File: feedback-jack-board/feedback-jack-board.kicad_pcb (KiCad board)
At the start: 2 copper layers, 80 x 36 mm, 6 parts, among them J1 Out, J2 Ret, J3 In, J4 Snd, J5 908140508, J6 Barrel_Jack_Switch

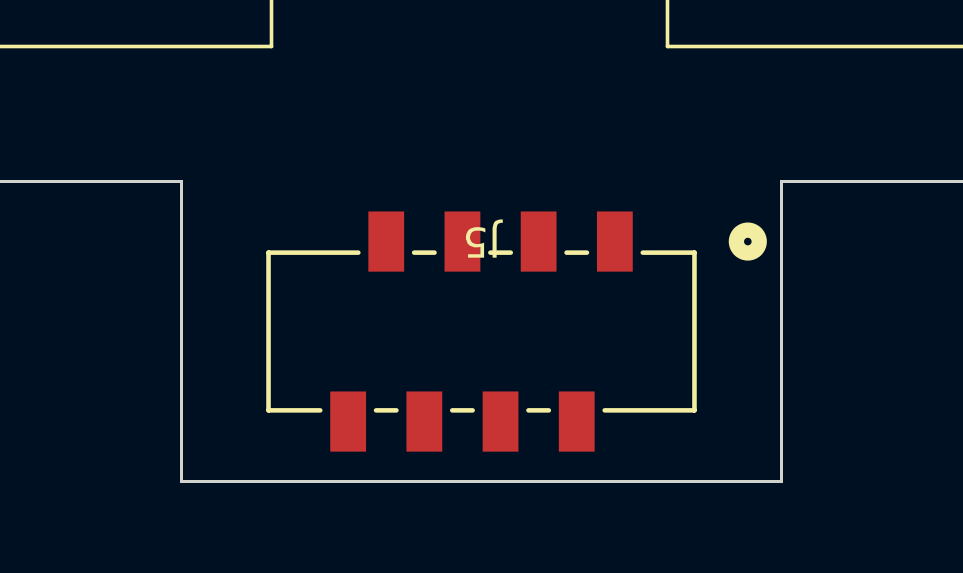
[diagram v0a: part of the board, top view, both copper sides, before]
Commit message: Rotate molex connector properly
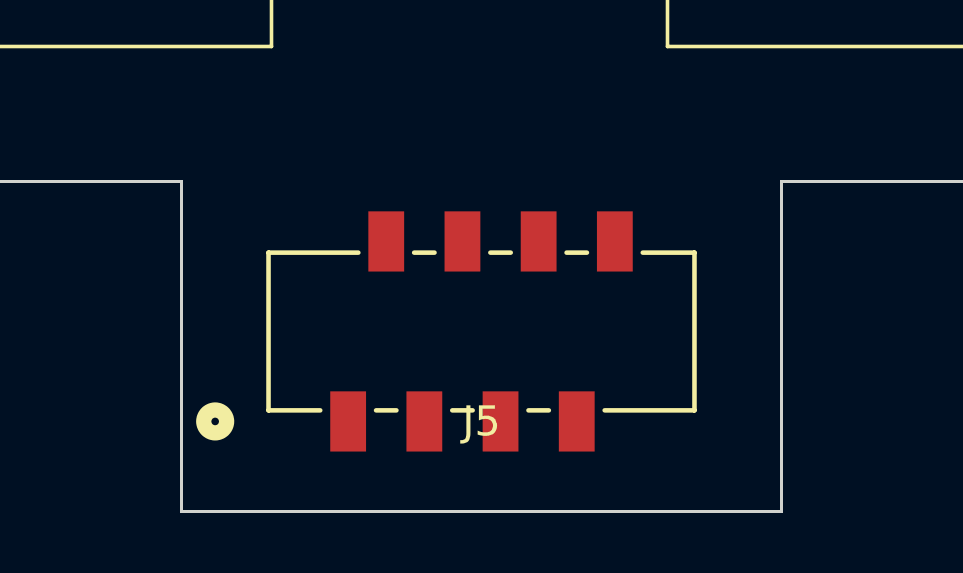
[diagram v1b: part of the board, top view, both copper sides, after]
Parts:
- turned J5 to 0 degrees
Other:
- board size 80 x 36 mm -> 80 x 37 mm
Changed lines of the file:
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@@
   )
   (footprint "molex-picoflex8:CONN_SDA-90814_08_MOL" (layer "F.Cu")
-    (at 100 76 180)
+    (at 100 76)
     (tags "908140508 ")
     (property "Sheetfile" "feedback-jack-board.kicad_sch")
     (property "Sheetname" "")
     (attr smd)
-    (fp_text reference "J5" (at 0 2.998099 180 unlocked) (layer "F.SilkS")
+    (fp_text reference "J5" (at 0 2.998099 unlocked) (layer "F.SilkS")
       (effects (font (size 1 1) (thickness 0.15)))
     )
-    (fp_text value "908140508" (at 0 2.998099 180 unlocked) (layer "F.Fab")
+    (fp_text value "908140508" (at 0 2.998099 unlocked) (layer "F.Fab")
       (effects (font (size 1 1) (thickness 0.15)))
     )
-    (fp_text user "${REFERENCE}" (at 0 2.998099 180 unlocked) (layer "F.Fab")
+    (fp_text user "${REFERENCE}" (at 0 2.998099 unlocked) (layer "F.Fab")
       (effects (font (size 1 1) (thickness 0.15)))
     )
@@
     (fp_line (start -6.9723 2.5019) (end 6.9723 2.5019) (layer "F.Fab") (width 0.0254))
     (fp_circle (center -4.445 4.903099) (end -4.064 4.903099) (layer "F.Fab") (width 0.508) (fill none))
-    (pad "1" smd rect (at -4.445 2.998099 180) (size 1.1938 2.0066) (layers "F.Cu" "F.Paste" "F.Mask")
+    (pad "1" smd rect (at -4.445 2.998099) (size 1.1938 2.0066) (layers "F.Cu" "F.Paste" "F.Mask")
       (net 17 "/Jack9V") (pinfunction "1") (pintype "unspecified"))
-    (pad "2" smd rect (at -3.175 -3.001902 180) (size 1.1938 2.0066) (layers "F.Cu" "F.Paste" "F.Mask")
+    (pad "2" smd rect (at -3.175 -3.001902) (size 1.1938 2.0066) (layers "F.Cu" "F.Paste" "F.Mask")
       (net 3 "/GND") (pinfunction "2") (pintype "unspecified"))
-    (pad "3" smd rect (at -1.905 2.998099 180) (size 1.1938 2.0066) (layers "F.Cu" "F.Paste" "F.Mask")
+    (pad "3" smd rect (at -1.905 2.998099) (size 1.1938 2.0066) (layers "F.Cu" "F.Paste" "F.Mask")
       (net 12 "/In") (pinfunction "3") (pintype "unspecified"))
-    (pad "4" smd rect (at -0.635 -3.001902 180) (size 1.1938 2.0066) (layers "F.Cu" "F.Paste" "F.Mask")
+    (pad "4" smd rect (at -0.635 -3.001902) (size 1.1938 2.0066) (layers "F.Cu" "F.Paste" "F.Mask")
       (net 9 "/Snd") (pinfunction "4") (pintype "unspecified"))
-    (pad "5" smd rect (at 0.635 2.998099 180) (size 1.1938 2.0066) (layers "F.Cu" "F.Paste" "F.Mask")
+    (pad "5" smd rect (at 0.635 2.998099) (size 1.1938 2.0066) (layers "F.Cu" "F.Paste" "F.Mask")
       (net 3 "/GND") (pinfunction "5") (pintype "unspecified"))
-    (pad "6" smd rect (at 1.905 -3.001902 180) (size 1.1938 2.0066) (layers "F.Cu" "F.Paste" "F.Mask")
+    (pad "6" smd rect (at 1.905 -3.001902) (size 1.1938 2.0066) (layers "F.Cu" "F.Paste" "F.Mask")
       (net 8 "/Ret") (pinfunction "6") (pintype "unspecified"))
-    (pad "7" smd rect (at 3.175 2.998099 180) (size 1.1938 2.0066) (layers "F.Cu" "F.Paste" "F.Mask")
+    (pad "7" smd rect (at 3.175 2.998099) (size 1.1938 2.0066) (layers "F.Cu" "F.Paste" "F.Mask")
       (net 4 "/Out") (pinfunction "7") (pintype "unspecified"))
-    (pad "8" smd rect (at 4.445 -3.001902 180) (size 1.1938 2.0066) (layers "F.Cu" "F.Paste" "F.Mask")
+    (pad "8" smd rect (at 4.445 -3.001902) (size 1.1938 2.0066) (layers "F.Cu" "F.Paste" "F.Mask")
       (net 18 "/Gnd") (pinfunction "8") (pintype "unspecified"))
+    (model "/Volumes/hdd/Projects/kicad/footprints/molex/ul_908140508/908140508.stp"
+      (offset (xyz 0 0 0))
+      (scale (xyz 1 1 1))
+      (rotate (xyz 0 0 0))
+    )
   )
   (gr_line (start 110 71) (end 139.5 71) (layer "Edge.Cuts") (width 0.1))
   (gr_line (start 59.5 45) (end 139.5 45) (layer "Edge.Cuts") (width 0.1))
   (gr_line (start 90 71) (end 59.5 71) (layer "Edge.Cuts") (width 0.1))
-  (gr_line (start 110 81) (end 90 81) (layer "Edge.Cuts") (width 0.1))
+  (gr_line (start 110 82) (end 90 82) (layer "Edge.Cuts") (width 0.1))
   (gr_line (start 59.5 71) (end 59.5 45) (layer "Edge.Cuts") (width 0.1))
   (gr_line (start 139.5 45) (end 139.5 71) (layer "Edge.Cuts") (width 0.1))
-  (gr_line (start 110 81) (end 110 71) (layer "Edge.Cuts") (width 0.1))
-  (gr_line (start 90 81) (end 90 71) (layer "Edge.Cuts") (width 0.1))
+  (gr_line (start 110 82) (end 110 71) (layer "Edge.Cuts") (width 0.1))
+  (gr_line (start 90 82) (end 90 71) (layer "Edge.Cuts") (width 0.1))
   (gr_rect (start 56.5 44) (end 143.5 156) (layer "User.8") (width 0.15) (fill none))
   (gr_rect (start 54.5 42) (end 145.5 158) (layer "User.8") (width 0.15) (fill none))

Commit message: Jacks board layout
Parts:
- added kibuzzard-67A4F0EE: G***, kibuzzard-67A4F0EE, F.Cu at (100.0, 61.0)
- added kibuzzard-67A4F113: G***, kibuzzard-67A4F113, F.Cu at (62.0, 70.0)
- added kibuzzard-67A4F12B: G***, kibuzzard-67A4F12B, F.Cu at (79.0, 70.0)
- added kibuzzard-67A4F13A: G***, kibuzzard-67A4F13A, F.Cu at (109.0, 70.0)
- added kibuzzard-67A4F143: G***, kibuzzard-67A4F143, F.Cu at (126.0, 70.0)
- added kibuzzard-67A4F1E7: G***, kibuzzard-67A4F1E7, B.Cu at (100.0, 65.0)
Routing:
- net /Out: track 0.00 -> 59.9 mm
- net /Jack9V: track 0.00 -> 54.4 mm
- net /Ret: track 0.00 -> 54.3 mm
- net /In: track 0.00 -> 38.1 mm
- net /Snd: track 0.00 -> 28.5 mm
- net /GND: track 0.00 -> 1.60 mm, vias 0 -> 1
- added copper zone on B.Cu, net /GND
- added copper zone on F.Cu, net /GND

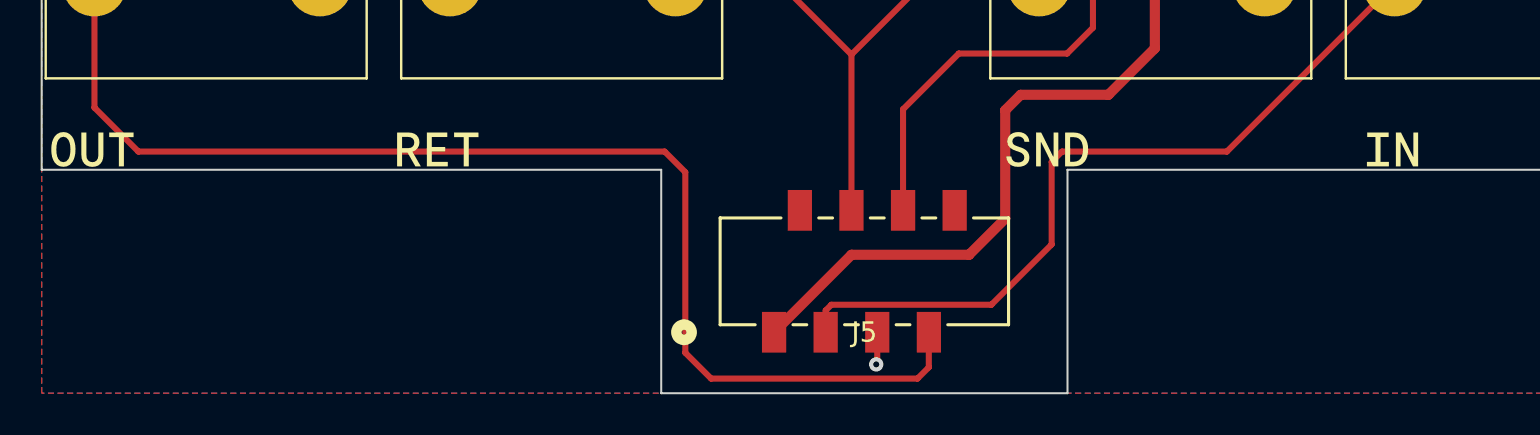
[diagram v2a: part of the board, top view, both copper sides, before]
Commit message: Jacks board ordered at aisler
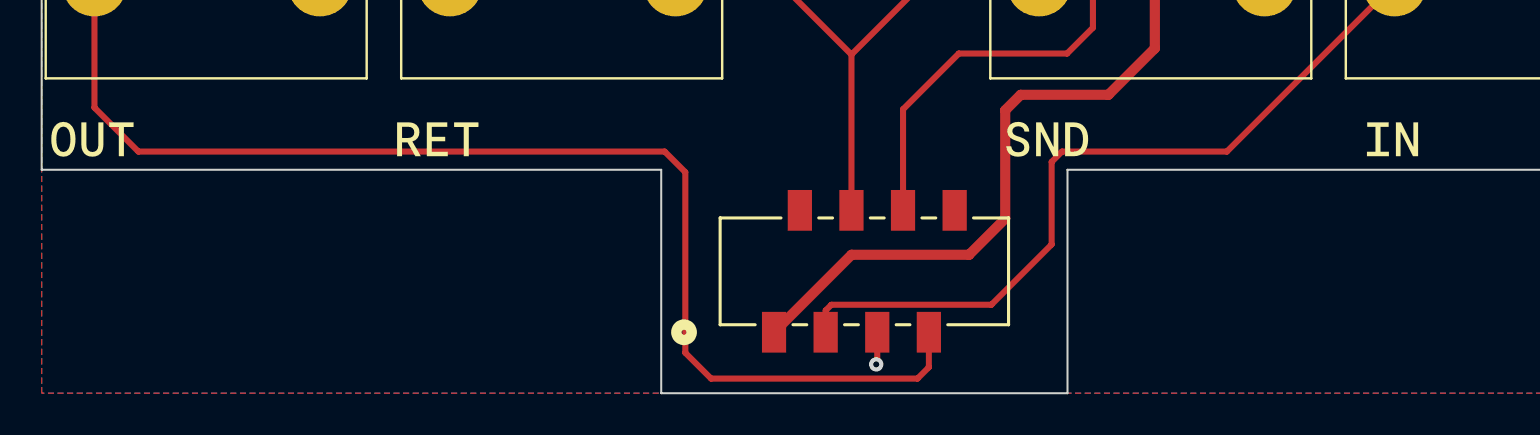
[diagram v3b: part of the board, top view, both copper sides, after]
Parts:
- moved kibuzzard-67A4F113 0.50 mm to (62.0, 69.5)
- moved kibuzzard-67A4F12B 0.50 mm to (79.0, 69.5)
- moved kibuzzard-67A4F13A 0.50 mm to (109.0, 69.5)
- moved kibuzzard-67A4F143 0.50 mm to (126.0, 69.5)
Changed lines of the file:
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@@
     (attr board_only exclude_from_pos_files exclude_from_bom)
     (fp_text reference "kibuzzard-67A4F0EE" (at 0 -3.821906) (layer "F.SilkS") hide
-      (effects (font (size 0 0)))
+      (effects (font (size 0 0) (thickness 0.15)))
     )
     (fp_text value "G***" (at 0 3.821906) (layer "F.SilkS") hide
-      (effects (font (size 0 0)))
+      (effects (font (size 0 0) (thickness 0.15)))
     )
     (fp_poly (pts
@@
   )
   (footprint "kibuzzard-67A4F143" (layer "F.Cu")
-    (at 126 70)
+    (at 126 69.5)
     (descr "Generated with KiBuzzard")
     (tags "kb_params=eyJBbGlnbm1lbnRDaG9pY2UiOiAiQ2VudGVyIiwgIkNhcExlZnRDaG9pY2UiOiAiIiwgIkNhcFJpZ2h0Q2hvaWNlIjogIiIsICJGb250Q29tYm9Cb3giOiAiTW9kZXJhdC1Nb25vLU1lZGl1bSIsICJIZWlnaHRDdHJsIjogIjEuNSIsICJMYXllckNvbWJvQm94IjogIkYuU2lsa1MiLCAiTXVsdGlMaW5lVGV4dCI6ICJJTiIsICJQYWRkaW5nQm90dG9tQ3RybCI6ICI1IiwgIlBhZGRpbmdMZWZ0Q3RybCI6ICI1IiwgIlBhZGRpbmdSaWdodEN0cmwiOiAiNSIsICJQYWRkaW5nVG9wQ3RybCI6ICI1IiwgIldpZHRoQ3RybCI6ICIxLjUifQ==")
     (attr board_only exclude_from_pos_files exclude_from_bom)
     (fp_text reference "kibuzzard-67A4F143" (at 0 -3.881438) (layer "F.SilkS") hide
-      (effects (font (size 0 0)))
+      (effects (font (size 0 0) (thickness 0.15)))
     )
     (fp_text value "G***" (at 0 3.881438) (layer "F.SilkS") hide
-      (effects (font (size 0 0)))
+      (effects (font (size 0 0) (thickness 0.15)))
     )
     (fp_poly (pts
@@
   )
   (footprint "kibuzzard-67A4F113" (layer "F.Cu")
-    (at 62 70)
+    (at 62 69.5)
     (descr "Generated with KiBuzzard")
     (tags "kb_params=eyJBbGlnbm1lbnRDaG9pY2UiOiAiQ2VudGVyIiwgIkNhcExlZnRDaG9pY2UiOiAiIiwgIkNhcFJpZ2h0Q2hvaWNlIjogIiIsICJGb250Q29tYm9Cb3giOiAiTW9kZXJhdC1Nb25vLU1lZGl1bSIsICJIZWlnaHRDdHJsIjogIjEuNSIsICJMYXllckNvbWJvQm94IjogIkYuU2lsa1MiLCAiTXVsdGlMaW5lVGV4dCI6ICJPVVQiLCAiUGFkZGluZ0JvdHRvbUN0cmwiOiAiNSIsICJQYWRkaW5nTGVmdEN0cmwiOiAiNSIsICJQYWRkaW5nUmlnaHRDdHJsIjogIjUiLCAiUGFkZGluZ1RvcEN0cmwiOiAiNSIsICJXaWR0aEN0cmwiOiAiMS41In0=")
     (attr board_only exclude_from_pos_files exclude_from_bom)
     (fp_text reference "kibuzzard-67A4F113" (at 0 -3.90525) (layer "F.SilkS") hide
-      (effects (font (size 0 0)))
+      (effects (font (size 0 0) (thickness 0.15)))
     )
     (fp_text value "G***" (at 0 3.90525) (layer "F.SilkS") hide
-      (effects (font (size 0 0)))
+      (effects (font (size 0 0) (thickness 0.15)))
     )
     (fp_poly (pts
@@
   )
   (footprint "kibuzzard-67A4F12B" (layer "F.Cu")
-    (at 79 70)
+    (at 79 69.5)
     (descr "Generated with KiBuzzard")
     (tags "kb_params=eyJBbGlnbm1lbnRDaG9pY2UiOiAiQ2VudGVyIiwgIkNhcExlZnRDaG9pY2UiOiAiIiwgIkNhcFJpZ2h0Q2hvaWNlIjogIiIsICJGb250Q29tYm9Cb3giOiAiTW9kZXJhdC1Nb25vLU1lZGl1bSIsICJIZWlnaHRDdHJsIjogIjEuNSIsICJMYXllckNvbWJvQm94IjogIkYuU2lsa1MiLCAiTXVsdGlMaW5lVGV4dCI6ICJSRVQiLCAiUGFkZGluZ0JvdHRvbUN0cmwiOiAiNSIsICJQYWRkaW5nTGVmdEN0cmwiOiAiNSIsICJQYWRkaW5nUmlnaHRDdHJsIjogIjUiLCAiUGFkZGluZ1RvcEN0cmwiOiAiNSIsICJXaWR0aEN0cmwiOiAiMS41In0=")
     (attr board_only exclude_from_pos_files exclude_from_bom)
     (fp_text reference "kibuzzard-67A4F12B" (at 0 -3.881438) (layer "F.SilkS") hide
-      (effects (font (size 0 0)))
+      (effects (font (size 0 0) (thickness 0.15)))
     )
     (fp_text value "G***" (at 0 3.881438) (layer "F.SilkS") hide
-      (effects (font (size 0 0)))
+      (effects (font (size 0 0) (thickness 0.15)))
     )
     (fp_poly (pts
@@
     (property "Sheetname" "")
     (attr smd)
-    (fp_text reference "J5" (at 0 2.998099 unlocked) (layer "F.SilkS")
+    (fp_text reference "J5" (at 0 2.998099 unlocked) (layer "F.SilkS") hide
       (effects (font (size 1 1) (thickness 0.15)))
     )
@@
   )
   (footprint "kibuzzard-67A4F13A" (layer "F.Cu")
-    (at 109 70)
+    (at 109 69.5)
     (descr "Generated with KiBuzzard")
     (tags "kb_params=eyJBbGlnbm1lbnRDaG9pY2UiOiAiQ2VudGVyIiwgIkNhcExlZnRDaG9pY2UiOiAiIiwgIkNhcFJpZ2h0Q2hvaWNlIjogIiIsICJGb250Q29tYm9Cb3giOiAiTW9kZXJhdC1Nb25vLU1lZGl1bSIsICJIZWlnaHRDdHJsIjogIjEuNSIsICJMYXllckNvbWJvQm94IjogIkYuU2lsa1MiLCAiTXVsdGlMaW5lVGV4dCI6ICJTTkQiLCAiUGFkZGluZ0JvdHRvbUN0cmwiOiAiNSIsICJQYWRkaW5nTGVmdEN0cmwiOiAiNSIsICJQYWRkaW5nUmlnaHRDdHJsIjogIjUiLCAiUGFkZGluZ1RvcEN0cmwiOiAiNSIsICJXaWR0aEN0cmwiOiAiMS41In0=")
     (attr board_only exclude_from_pos_files exclude_from_bom)
     (fp_text reference "kibuzzard-67A4F13A" (at 0 -3.90525) (layer "F.SilkS") hide
-      (effects (font (size 0 0)))
+      (effects (font (size 0 0) (thickness 0.15)))
     )
     (fp_text value "G***" (at 0 3.90525) (layer "F.SilkS") hide
-      (effects (font (size 0 0)))
+      (effects (font (size 0 0) (thickness 0.15)))
     )
     (fp_poly (pts
@@
     (attr board_only exclude_from_pos_files exclude_from_bom)
     (fp_text reference "kibuzzard-67A4F1E7" (at 0 8.3058) (layer "B.SilkS") hide
-      (effects (font (size 0 0)) (justify mirror))
+      (effects (font (size 0 0) (thickness 0.15)) (justify mirror))
     )
     (fp_text value "G***" (at 0 -8.3058) (layer "B.SilkS") hide
-      (effects (font (size 0 0)) (justify mirror))
-    )
-    (fp_poly (pts
+      (effects (font (size 0 0) (thickness 0.15)) (justify mirror))
+    )
+    (fp_poly (pts
